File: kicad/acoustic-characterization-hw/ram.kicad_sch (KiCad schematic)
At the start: 3 parts, among them IC1 ECP5-BGA256, U5 MT41K64M16TW-107_J-TR

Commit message: [kicad] Connected DDR3L bus, added info on FPGA and ddr pin functionality (next) add filtering circuitry for DDR power pins
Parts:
- removed unit 7 of IC1
- added C32, C33: 1uF, Capacitor_SMD:C_0402_1005Metric, symbol Device:C
- added C34, C35: 22uF, Capacitor_SMD:C_0603_1608Metric, symbol Device:C
- added FB2, FB3: 600R, Inductor_SMD:L_0402_1005Metric, symbol Device:L_Small
- R24: value 240 -> R_Small
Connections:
- net ECP5_VREF is gone; now on net V_DRR3L_0.675: U5.H1 (VREFDQ), U5.M8 (VREFCA)
- net GND: now also C32.2, C33.2, C34.2, C35.2
- net RAM_A0: now also IC1.N4 (PL38A/LDQ44)
- net RAM_A1: now also IC1.N3 (PL35D)
- net RAM_A10: now also IC1.K5 (PL29B)
- net RAM_A11: now also IC1.K4 (PL29A/GR_PCLK6_0)
- net RAM_A12: now also IC1.M2 (PL26D/PCLKC6_0)
- net RAM_A13: now also IC1.M1 (PL26C/PCLKT6_0)
- net RAM_A14: now also IC1.L2 (PL26B/PCLKC6_1)
- net RAM_A15: now also IC1.L1 (PL26A/LDQ32/PCLKT6_1)
- net RAM_A2: now also IC1.M4 (PL35C)
- net RAM_A3: now also IC1.P1 (PL35A)
- net RAM_A4: now also IC1.M3 (PL32D)
- net RAM_A5: now also IC1.L3 (PL32C)
- net RAM_A6: now also IC1.P2 (PL32B/LDQSN32)
- net RAM_A7: now also IC1.N1 (PL32A/LDQS32)
- net RAM_A8: now also IC1.L5 (PL29D)
- net RAM_A9: now also IC1.L4 (PL29C/PL29C)
- net RAM_BA0: now also IC1.R5 (PL44A/LDQS44)
- net RAM_BA1: now also IC1.T2 (PL38D)
- net RAM_BA2: now also IC1.R2 (PL38C)
- net RAM_CAS#: now also IC1.P4 (PL41A)
- net RAM_CK+: now also IC1.P5 (PL47D/LLC_GPLL0C_IN)
- net RAM_CK-: now also IC1.N6 (PL47B)
- net RAM_CKE: now also IC1.M6 (PL47A)
- net RAM_CS#: now also IC1.P6 (PL47C/LLC_GPLL0T_IN)
- net RAM_D0: now also IC1.B16 (PR2A/RDQ8)
- net RAM_D1: now also IC1.B15 (PR2B/S0_IN)
- net RAM_D10: now also IC1.H14 (PR14D)
- net RAM_D11: now also IC1.H12 (PR17A)
- net RAM_D12: now also IC1.H13 (PR17B)
- net RAM_D13: now also IC1.J13 (PR17C)
- net RAM_D14: now also IC1.J12 (PR17D)
- net RAM_D15: now also IC1.J14 (PR20C/GR_PCLK2_1)
- net RAM_D2: now also IC1.C14 (PR2C)
- net RAM_D3: now also IC1.D14 (PR2D)
- net RAM_D4: now also IC1.C16 (PR5A)
- net RAM_D5: now also IC1.C15 (PR5B)
- net RAM_D6: now also IC1.E14 (PR5C)
- net RAM_D7: now also IC1.F14 (PR5D)
- net RAM_D8: now also IC1.F16 (PR14A/RDQ20)
- net RAM_D9: now also IC1.G15 (PR14B)
- net RAM_LDM: now also IC1.T3 (PL41D)
- net RAM_LDQS+: now also IC1.D16 (PR8A/RDQS8), U5.F3 (LDQS); no longer U5.C7 (UDQS)
- net RAM_LDQS-: now also IC1.E15 (PR8B/RDQSN8), U5.G3 (LDQS#); no longer U5.B7 (UDQS#)
- net RAM_ODT: now also IC1.R4 (PL41C)
- net RAM_RAS#: now also IC1.R3 (PL41B)
- net RAM_RESET#: now also IC1.M5 (PL44C)
- net RAM_UDM: now also IC1.T4 (PL44B/LDQSN44)
- net RAM_UDQS+: now also IC1.G16 (PR20A/RDQS20), U5.C7 (UDQS); no longer U5.F3 (LDQS)
- net RAM_UDQS-: now also IC1.H15 (PR20B/RDQS20), U5.B7 (UDQS#); no longer U5.G3 (LDQS#)
- net RAM_WE#: now also IC1.N5 (PL44D)
- net V_DRR3L_0.675: now reaches IC1.G14 (PR14C/VREF1_2)
- net V_DRR3L_0.675: now also IC1.R1 (PL35B/VREF1_6)
- net V_DDR3L_1.35: now reaches IC1.H11 (VCCIO2_1)
- net V_DDR3L_1.35: now also IC1.J11 (VCCIO2_2), IC1.J6 (VCCIO6_1), IC1.J7 (VCCIO6_2), FB2.2, FB3.2
- net RAM_VDD: no longer names the net of U5.B2 (VDD[9]), U5.D9 (VDD), U5.G7 (VDD), U5.K2 (VDD), U5.K8 (VDD), U5.N1 (VDD), U5.N9 (VDD), U5.R1 (VDD), U5.R9 (VDD)
- net RAM_VDD: now also C32.1, C34.1, FB2.1
- net RAM_VDDQ: no longer names the net of U5.A1 (VDDQ[9]), U5.A8 (VDDQ), U5.C1 (VDDQ), U5.C9 (VDDQ), U5.D2 (VDDQ), U5.E9 (VDDQ), U5.F1 (VDDQ), U5.H2 (VDDQ), U5.H9 (VDDQ)
- net RAM_VDDQ: now also C33.1, C35.1, FB3.1
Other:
- note added: "TODO - Add appropriate filtering circuitry and decoupling"
- note added: "TODO: - When doing actual routing from banks make sure to change pin assignments for appropriate routing"
- note added: "VREFCA, VREFDQ: - reference voltages separated for data and control/command address - Should be held at 0.675 V"
- note added: "Vref: - The DDR-logic requires an external 0.75 Volts (SSTL-15 standard). - External resistive divider required Vcc: The DDRL-ram requires a 1.35 V supply voltage. - LDO / buck converter DQS-pins - Upper / Lower 8-bit synchronization for data Data-pins: - upper 8 and lower 8 bits must belong to same DQS pins Address / config pins - can be any DQ pins in the bank"
- moved on the sheet: IC1D, IC1F, R24, U5

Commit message: [kicad] re-added passive values after accidental removal
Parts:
- R24: value R_Small -> 240
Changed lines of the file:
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@@
 			)
 		)
-		(property "Value" "R_Small"
+		(property "Value" "240"
 			(at 240.538 67.31 90)
 			(effects

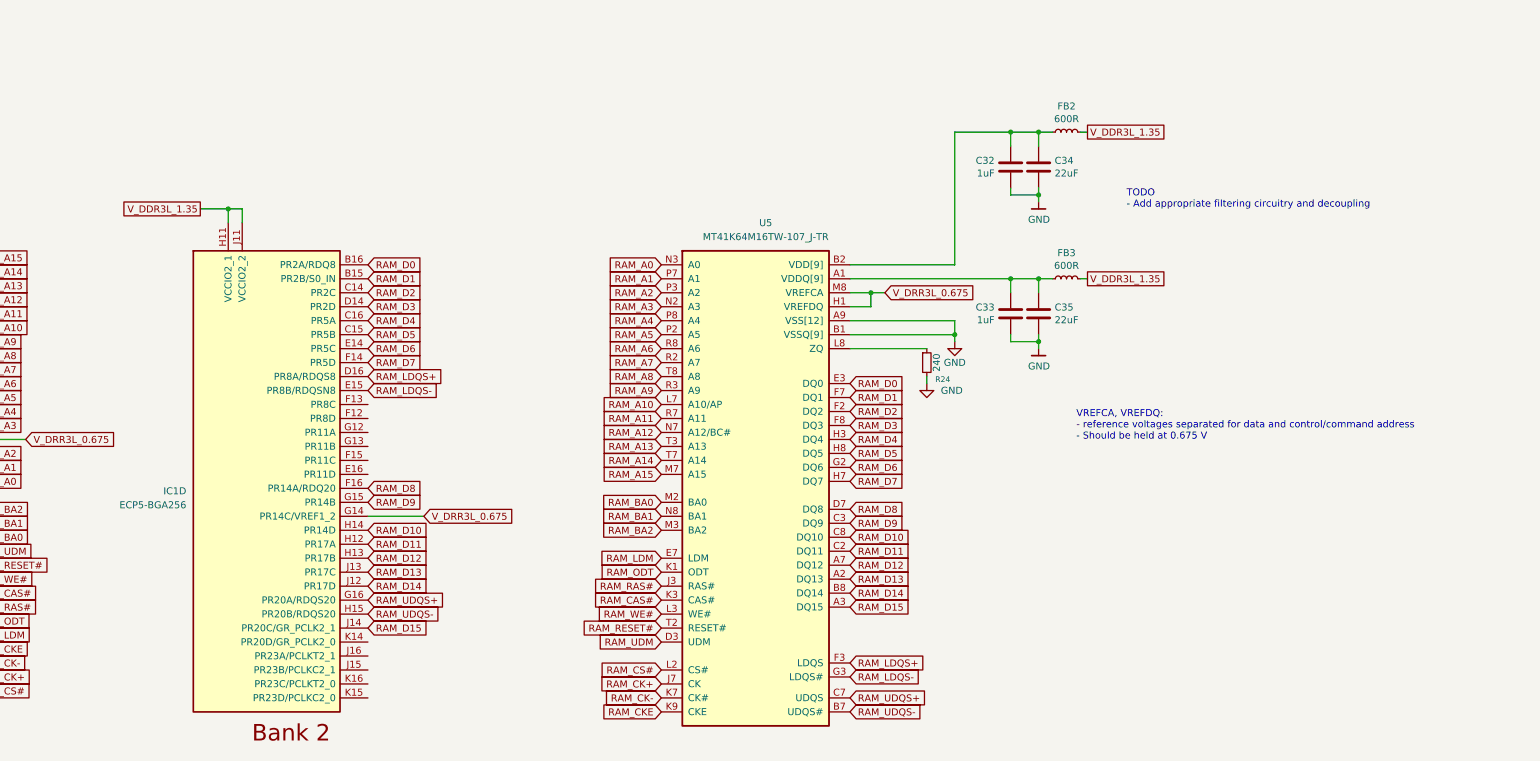
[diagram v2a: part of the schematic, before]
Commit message: [simulations] Added buck converter simulations (next) Completely understand voltage swing reasons and stabilize
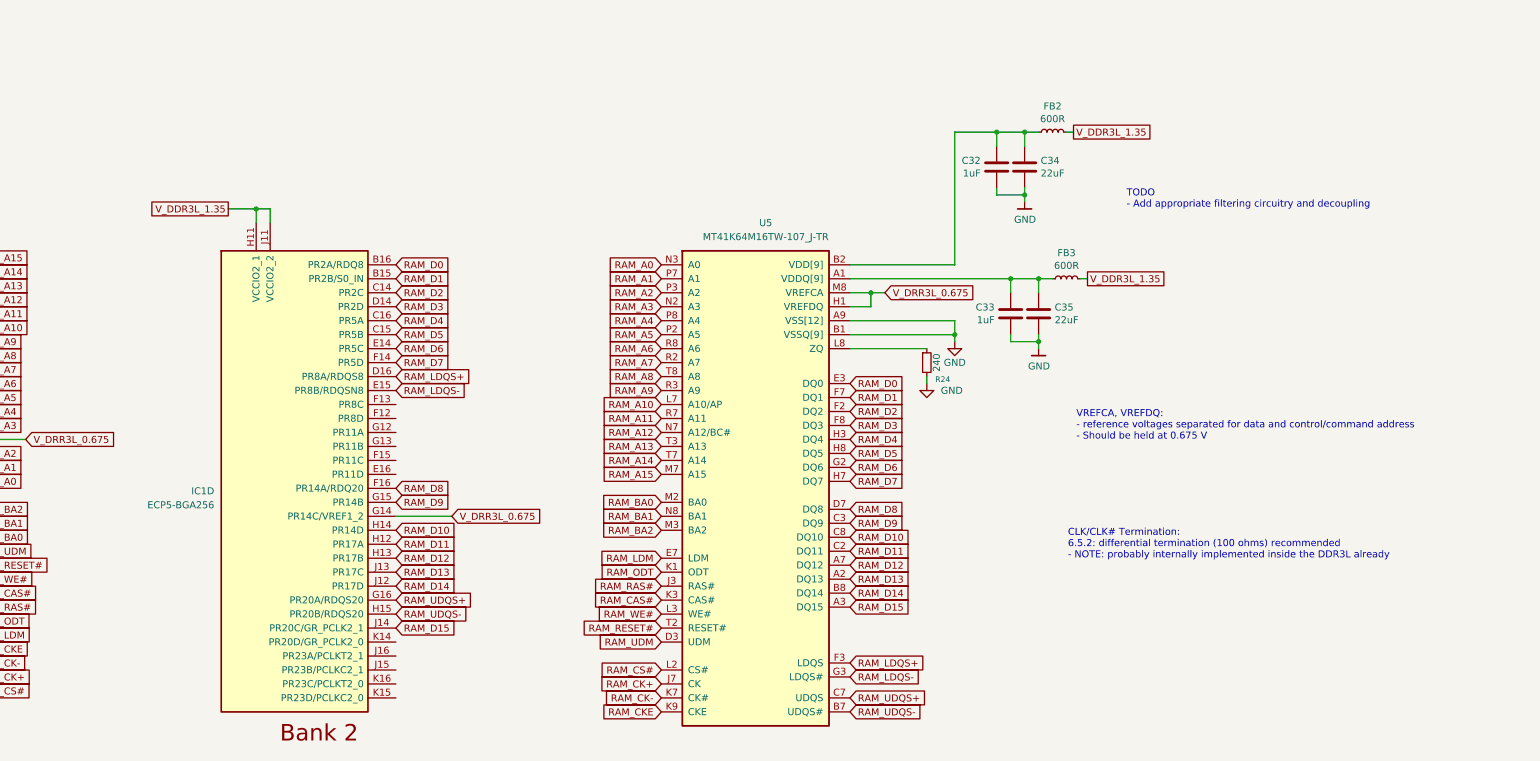
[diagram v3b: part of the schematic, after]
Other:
- note added: "CLK/CLK# Termination: 6.5.2: differential termination (100 ohms) recommended - NOTE: probably internally implemented inside the DDR3L already"
- moved on the sheet: C32, C34, FB2, IC1D
